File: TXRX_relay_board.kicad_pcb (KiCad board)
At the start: 2 copper layers, 100 x 82 mm, 80 parts, among them J1 Screw_Terminal_01x02, J2 Conn_01x08, J3 IN, J4 IN_RF_Deck, J5 OUT_RF_Deck, J6 OUT, K1 RT314A05, K2 RT314A05, Q1 BC807, Q2 BC807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

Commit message: Ready to Order
Minor updates in preparation to order PCBs and components
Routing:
- net Net-(Q4-E): track 23.5 -> 26.5 mm
- net +12V: track 171.3 -> 169.1 mm
- net FWD_PWR: track 45.9 -> 44.7 mm
- net Rel2: track 98.1 -> 97.2 mm
- net Net-(J4-In): track 10.5 -> 9.56 mm
- net +5V: track 58.5 -> 57.6 mm
- net Net-(R16-Pad2): track 25.8 -> 25.1 mm
- net Rel1: track 64.2 -> 63.6 mm
- net Bias: track 21.1 -> 20.6 mm
- net Net-(U1--): track 12.9 -> 12.4 mm

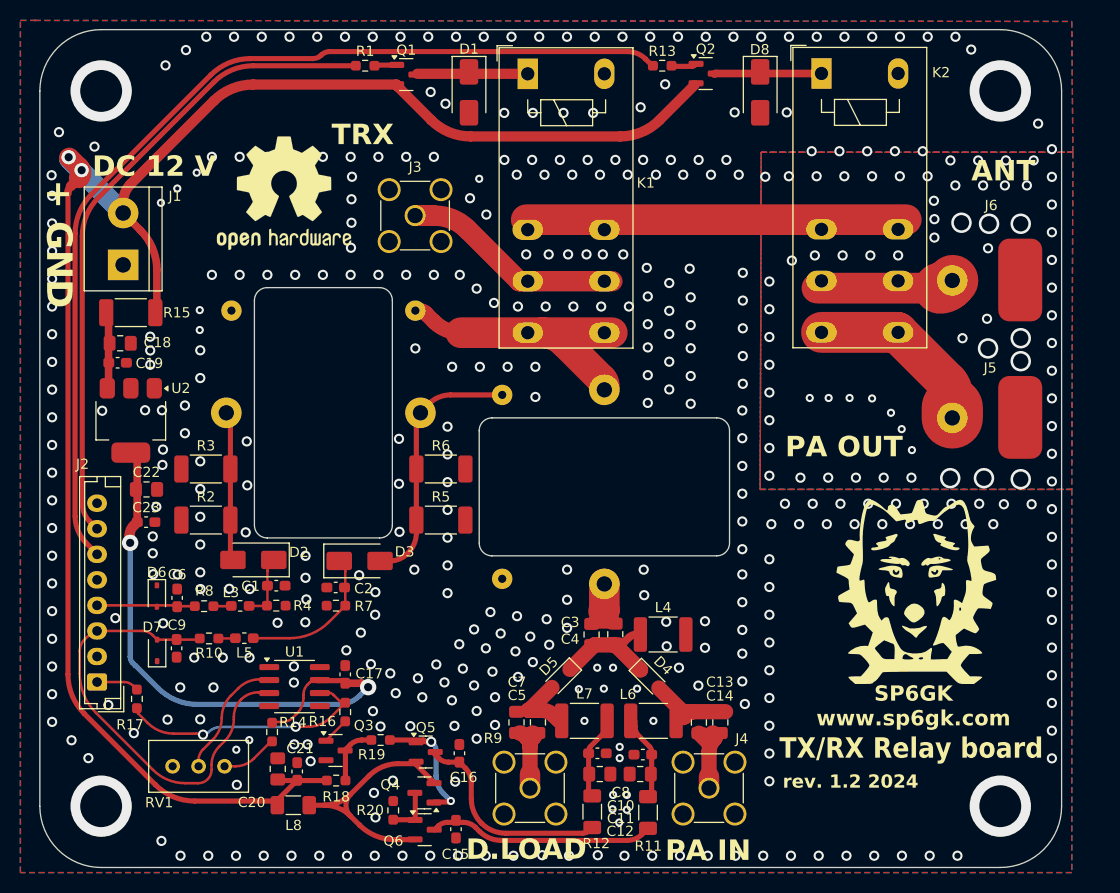
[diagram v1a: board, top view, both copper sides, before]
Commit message: All checks done, BOM updated
All ERC and DRC checks have been run, and erros and or warnings resolved.
BOM fully updated with Manufacturer part numbers (MPN) ready for order placement
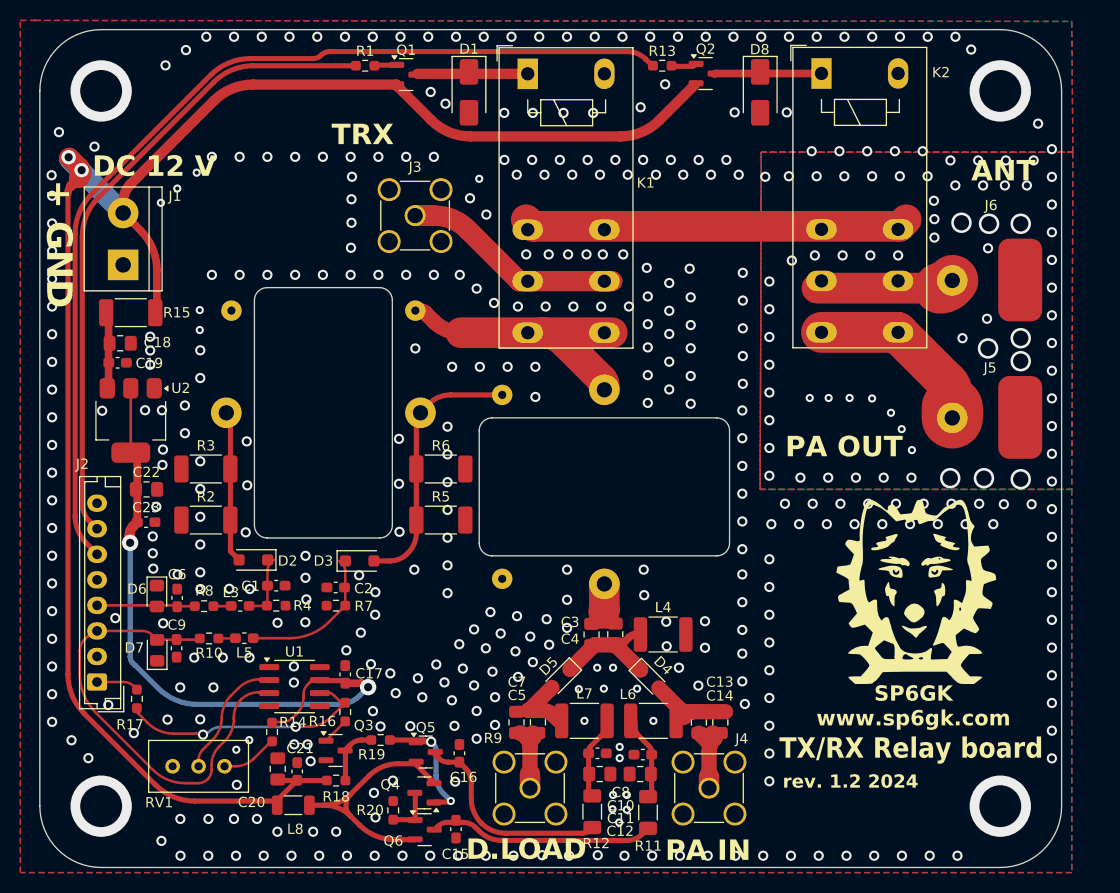
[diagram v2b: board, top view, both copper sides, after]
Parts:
- removed REF**: OSHW-Logo2_14.6x12mm_SilkScreen, Symbol:OSHW-Logo2_14.6x12mm_SilkScreen
- D2, D3: value Schottky -> 1N4148; footprint Diode_SMD:D_SMA -> Diode_SMD:D_SOD-123F
- D6, D7: footprint Diode_SMD:D_SOD-323 -> Diode_SMD:D_0805_2012Metric_Pad1.15x1.40mm_HandSolder
- L3, L5: value L_Small -> 1uH
- L4, L6, L7: value 1m -> 1mH
- L8: value 100u -> 100uH; footprint Capacitor_SMD:C_1206_3216Metric_Pad1.33x1.80mm_HandSolder -> Inductor_SMD:L_1206_3216Metric
- moved OSHW 3.00 mm to (87.2, 71.5)
- renumbered REF** to OSHW
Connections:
- K1 pad A1: Net-(D1-K) -> GND
- K1 pad A2: GND -> Net-(D1-K)
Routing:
- net +5V: track 57.6 -> 63.9 mm
- net Net-(D2-A): track 13.3 -> 14.3 mm
- net Net-(K1-Pad12): track 37.2 -> 37.8 mm
- net GND: vias 442 -> 449
